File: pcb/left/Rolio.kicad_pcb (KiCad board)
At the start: 2 copper layers, 141.5 x 83 mm, 110 parts, among them Q1 AO3400A, SW4 SW_DIP_x01

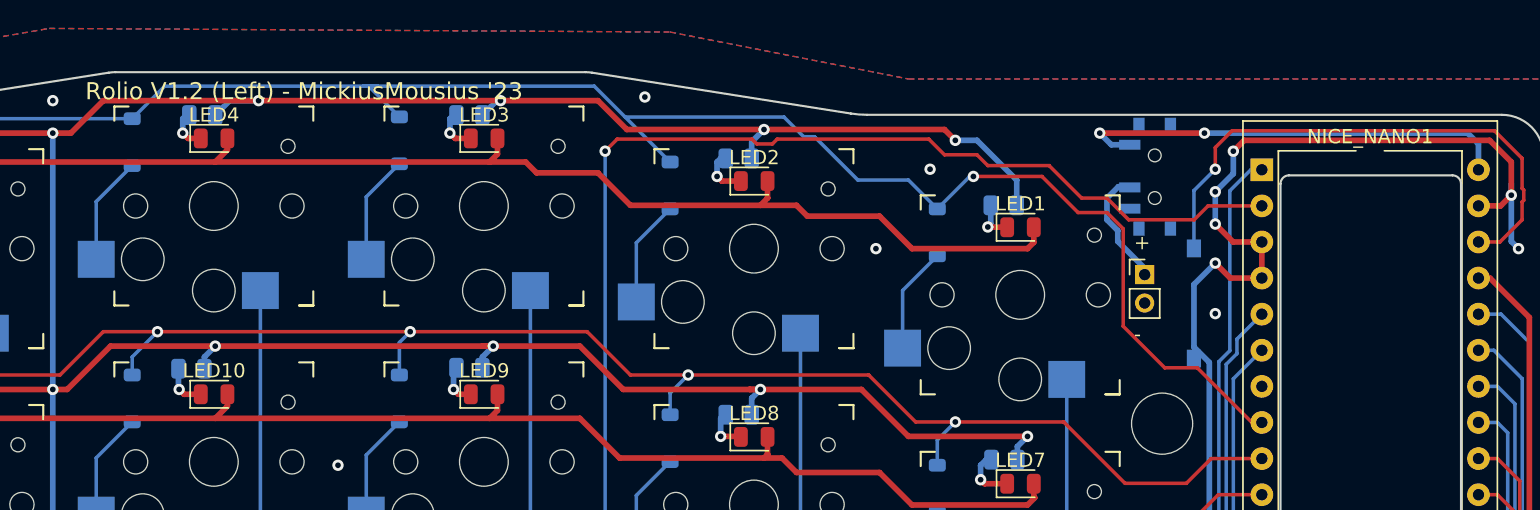
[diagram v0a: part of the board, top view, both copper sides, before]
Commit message: Develop (#18) Update to 1.1
* Remove SLS option

* Update the landing page

* Update PCB to have nicer soldering pads for the battery

* Update the right PCB to have a nicer set of solder pads for the battery

* Update 3D models exports from KiCAD

* Update JLCPCB production files

* Update the CNC production files & instructions

* Update FDM resources

* Add information about the Mikoto controller

* Update the display information page

* Update the shield readme
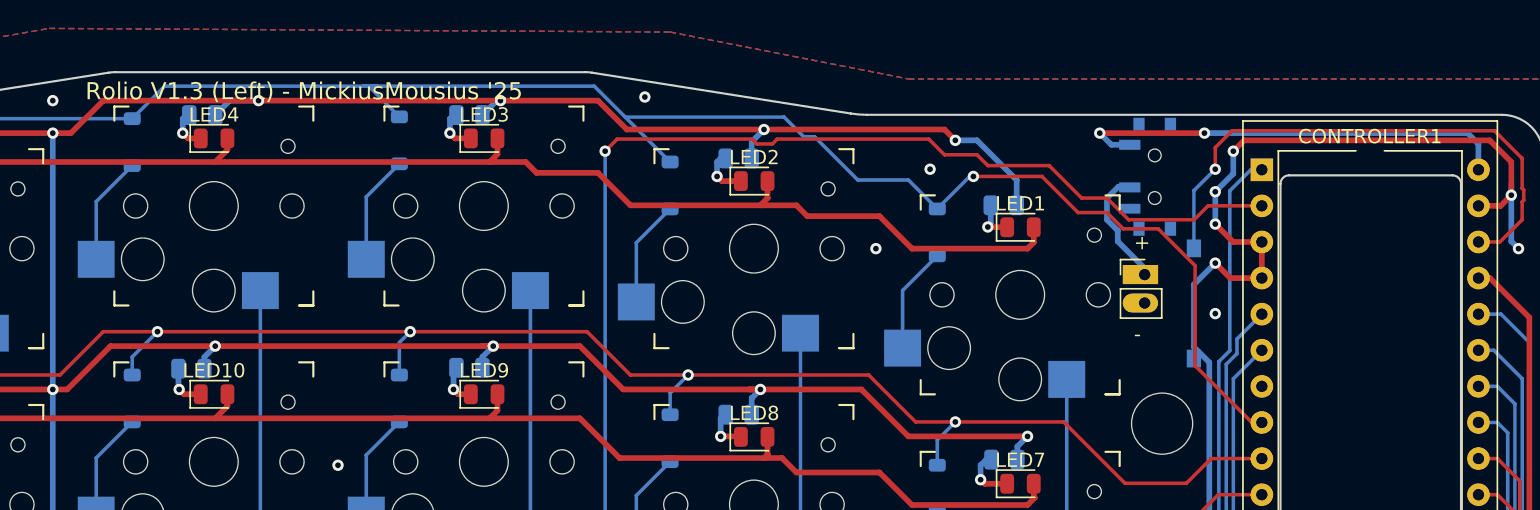
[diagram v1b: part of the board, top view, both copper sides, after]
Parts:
- renumbered NICE_NANO1 to CONTROLLER1
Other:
- board text added: "Rolio V1.3 (Left) - MickiusMousius '25"
- board text removed: "Rolio V1.2 (Left) - MickiusMousius '23"
